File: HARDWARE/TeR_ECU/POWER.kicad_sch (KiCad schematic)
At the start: 8 parts, among them U10 LM1117MP-3.3, U2 TSR_1-2450

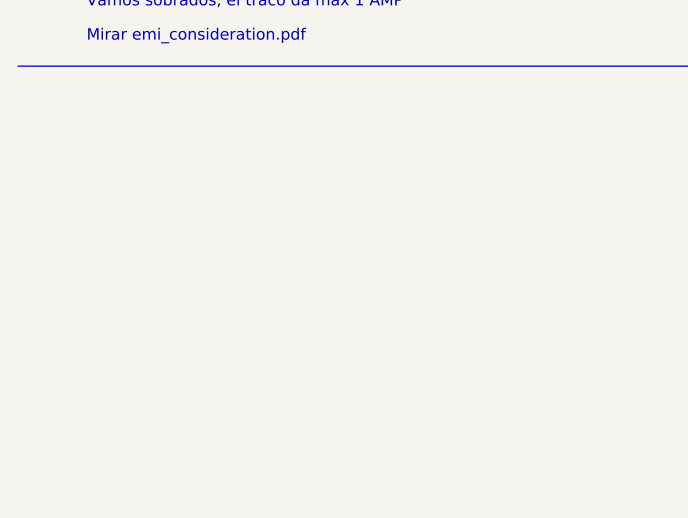
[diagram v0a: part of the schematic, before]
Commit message: Advanced design and added IMU/GPS moduleç
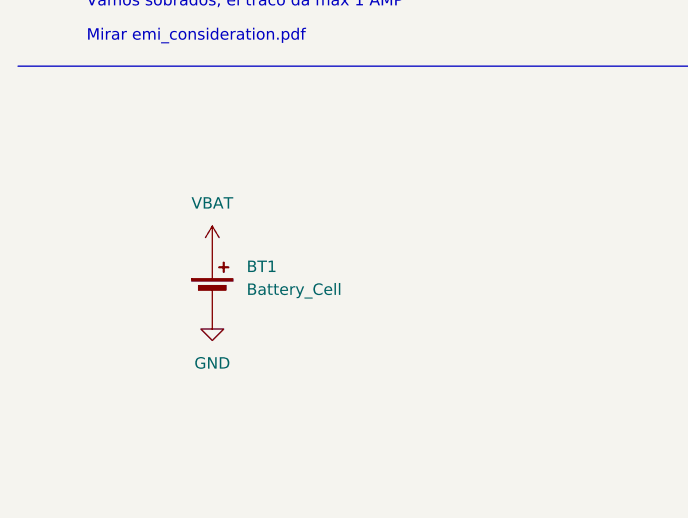
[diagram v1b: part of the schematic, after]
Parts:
- added BT1: Battery_Cell, symbol Device:Battery_Cell
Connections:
- net GND: now also BT1.2 (-)
- new net VBAT: BT1.1 (+)
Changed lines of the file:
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@@
 			(project "TeR_ECU"
 				(path "/84413845-c4f3-4743-bcd2-a67649c90902/b76a95f3-584c-4daf-bbe9-70945b593e94"
-					(reference "#PWR05")
+					(reference "#PWR033")
 					(unit 1)
 				)
@@
 			(project "TeR_ECU"
 				(path "/84413845-c4f3-4743-bcd2-a67649c90902/b76a95f3-584c-4daf-bbe9-70945b593e94"
-					(reference "U5")
+					(reference "U3")
 					(unit 1)
 				)
@@
 			(project "TeR_ECU"
 				(path "/84413845-c4f3-4743-bcd2-a67649c90902/b76a95f3-584c-4daf-bbe9-70945b593e94"
-					(reference "C22")
+					(reference "C12")
 					(unit 1)
 				)
@@
 			(project "TeR_ECU"
 				(path "/84413845-c4f3-4743-bcd2-a67649c90902/b76a95f3-584c-4daf-bbe9-70945b593e94"
-					(reference "#PWR044")
+					(reference "#PWR030")
+					(unit 1)
+				)
+			)
+		)
+	)
+	(symbol
+		(lib_name "GND_1")
+		(lib_id "power:GND")
+		(at 34.29 96.52 0)
+		(unit 1)
+		(exclude_from_sim no)
+		(in_bom yes)
+		(on_board yes)
+		(dnp no)
+		(fields_autoplaced yes)
+		(property "Reference" "#PWR036"
+			(at 34.29 102.87 0)
+			(effects
+				(font
+					(size 1.27 1.27)
+				)
+				(hide yes)
+			)
+		)
+		(property "Value" "GND"
+			(at 34.29 101.6 0)
+			(effects
+				(font
+					(size 1.27 1.27)
+				)
+			)
+		)
+		(property "Footprint" ""
+			(at 34.29 96.52 0)
+			(effects
+				(font
+					(size 1.27 1.27)
+				)
+				(hide yes)
+			)
+		)
+		(property "Datasheet" ""
+			(at 34.29 96.52 0)
+			(effects
+				(font
+					(size 1.27 1.27)
+				)
+				(hide yes)
+			)
+		)
+		(property "Description" "Power symbol creates a global label with name \"GND\" , ground"
+			(at 34.29 96.52 0)
+			(effects
+				(font
+					(size 1.27 1.27)
+				)
+				(hide yes)
+			)
+		)
+		(pin "1"
+		)
+		(instances
+			(project ""
+				(path "/84413845-c4f3-4743-bcd2-a67649c90902/b76a95f3-584c-4daf-bbe9-70945b593e94"
+					(reference "#PWR036")
 					(unit 1)
 				)
@@
 			(project "TeR_ECU"
 				(path "/84413845-c4f3-4743-bcd2-a67649c90902/b76a95f3-584c-4daf-bbe9-70945b593e94"
-					(reference "#PWR06")
+					(reference "#PWR037")
+					(unit 1)
+				)
+			)
+		)
+	)
+	(symbol
+		(lib_id "Device:Battery_Cell")
+		(at 34.29 93.98 0)
+		(unit 1)
+		(exclude_from_sim no)
+		(in_bom yes)
+		(on_board yes)
+		(dnp no)
+		(fields_autoplaced yes)
+		(property "Reference" "BT1"
+			(at 38.1 90.8684 0)
+			(effects
+				(font
+					(size 1.27 1.27)
+				)
+				(justify left)
+			)
+		)
+		(property "Value" "Battery_Cell"
+			(at 38.1 93.4084 0)
+			(effects
+				(font
+					(size 1.27 1.27)
+				)
+				(justify left)
+			)
+		)
+		(property "Footprint" ""
+			(at 34.29 92.456 90)
+			(effects
+				(font
+					(size 1.27 1.27)
+				)
+				(hide yes)
+			)
+		)
+		(property "Datasheet" "~"
+			(at 34.29 92.456 90)
+			(effects
+				(font
+					(size 1.27 1.27)
+				)
+				(hide yes)
+			)
+		)
+		(property "Description" "Single-cell battery"
+			(at 34.29 93.98 0)
+			(effects
+				(font
+					(size 1.27 1.27)
+				)
+				(hide yes)
+			)
+		)
+		(pin "1"
+		)
+		(pin "2"
+		)
+		(instances
+			(project ""
+				(path "/84413845-c4f3-4743-bcd2-a67649c90902/b76a95f3-584c-4daf-bbe9-70945b593e94"
+					(reference "BT1")
 					(unit 1)
 				)
@@
 			(project "TeR_ECU"
 				(path "/84413845-c4f3-4743-bcd2-a67649c90902/b76a95f3-584c-4daf-bbe9-70945b593e94"
-					(reference "C19")
+					(reference "C9")
 					(unit 1)
 				)
@@
 			(project "TeR_ECU"
 				(path "/84413845-c4f3-4743-bcd2-a67649c90902/b76a95f3-584c-4daf-bbe9-70945b593e94"
-					(reference "#PWR046")
+					(reference "#PWR032")
 					(unit 1)
 				)
@@
 			(project "TeR_ECU"
 				(path "/84413845-c4f3-4743-bcd2-a67649c90902/b76a95f3-584c-4daf-bbe9-70945b593e94"
-					(reference "C20")
+					(reference "C10")
 					(unit 1)
 				)
@@
 			(project "TeR_ECU"
 				(path "/84413845-c4f3-4743-bcd2-a67649c90902/b76a95f3-584c-4daf-bbe9-70945b593e94"
-					(reference "#PWR07")
+					(reference "#PWR034")
 					(unit 1)
 				)
@@
 			(project "TeR_ECU"
 				(path "/84413845-c4f3-4743-bcd2-a67649c90902/b76a95f3-584c-4daf-bbe9-70945b593e94"
-					(reference "#PWR042")
+					(reference "#PWR028")
 					(unit 1)
 				)
@@
 			(project "TeR_ECU"
 				(path "/84413845-c4f3-4743-bcd2-a67649c90902/b76a95f3-584c-4daf-bbe9-70945b593e94"
-					(reference "C21")
+					(reference "C11")
 					(unit 1)
 				)
@@
 			(project "TeR_ECU"
 				(path "/84413845-c4f3-4743-bcd2-a67649c90902/b76a95f3-584c-4daf-bbe9-70945b593e94"
-					(reference "#PWR039")
+					(reference "#PWR027")
 					(unit 1)
 				)
@@
 			(project "TeR_ECU"
 				(path "/84413845-c4f3-4743-bcd2-a67649c90902/b76a95f3-584c-4daf-bbe9-70945b593e94"
-					(reference "U1")
+					(reference "U4")
 					(unit 1)
 				)
@@
 	)
 	(symbol
+		(lib_id "power:VCC")
+		(at 34.29 88.9 0)
+		(unit 1)
+		(exclude_from_sim no)
+		(in_bom yes)
+		(on_board yes)
+		(dnp no)
+		(fields_autoplaced yes)
+		(property "Reference" "#PWR035"
+			(at 34.29 92.71 0)
+			(effects
+				(font
+					(size 1.27 1.27)
+				)
+				(hide yes)
+			)
+		)
+		(property "Value" "VBAT"
+			(at 34.29 83.82 0)
+			(effects
+				(font
+					(size 1.27 1.27)
+				)
+			)
+		)
+		(property "Footprint" ""
+			(at 34.29 88.9 0)
+			(effects
+				(font
+					(size 1.27 1.27)
+				)
+				(hide yes)
+			)
+		)
+		(property "Datasheet" ""
+			(at 34.29 88.9 0)
+			(effects
+				(font
+					(size 1.27 1.27)
+				)
+				(hide yes)
+			)
+		)
+		(property "Description" "Power symbol creates a global label with name \"VBAT\""
+			(at 34.29 88.9 0)
+			(effects
+				(font
+					(size 1.27 1.27)
+				)
+				(hide yes)
+			)
+		)
+		(pin "1"
+		)
+		(instances
+			(project ""
+				(path "/84413845-c4f3-4743-bcd2-a67649c90902/b76a95f3-584c-4daf-bbe9-70945b593e94"
+					(reference "#PWR035")
+					(unit 1)
+				)
+			)
+		)
+	)
+	(symbol
 		(lib_id "power:+24V")
 		(at 180.975 39.37 270)
@@
 			(project "TeR_ECU"
 				(path "/84413845-c4f3-4743-bcd2-a67649c90902/b76a95f3-584c-4daf-bbe9-70945b593e94"
-					(reference "#PWR049")
+					(reference "#PWR029")
 					(unit 1)
 				)
@@
 			(project "TeR_ECU"
 				(path "/84413845-c4f3-4743-bcd2-a67649c90902/b76a95f3-584c-4daf-bbe9-70945b593e94"
-					(reference "#PWR045")
-					(unit 1)
-				)
+					(reference "#PWR031")
+					(unit 1)
+				)

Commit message: Cool things
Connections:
- net 24V_IN renamed 24_VIN
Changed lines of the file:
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@@
 		(color 0 0 0 0)
 	)
+	(wire
+		(pts
+			(xy 151.13 39.37) (xy 161.29 39.37)
+		)
+		(stroke
+			(width 0)
+			(type default)
+		)
+	)
 	(polyline
 		(pts
@@
 		(pts
 			(xy 46.99 45.72) (xy 46.99 41.91)
-		)
-		(stroke
-			(width 0)
-			(type default)
-		)
-	)
-	(wire
-		(pts
-			(xy 161.29 39.37) (xy 151.765 39.37)
 		)
 		(stroke
@@
 		)
 	)
-	(hierarchical_label "24V_IN"
+	(global_label "24_VIN"
 		(shape input)
-		(at 151.765 39.37 180)
+		(at 151.13 39.37 180)
 		(fields_autoplaced yes)
 		(effects
@@
 			(justify right)
 		)
-	)
+		(property "Intersheetrefs" "${INTERSHEET_REFS}"
+			(at 141.7343 39.37 0)
+			(effects
+				(font
+					(size 1.27 1.27)
+				)
+				(justify right)
+				(hide yes)
+			)
+		)
+	)

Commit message: Quick changes, go to start layouting
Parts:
- removed BT1: Battery_Cell, symbol Device:Battery_Cell
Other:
- note removed: "Vamos sobrados, el traco da max 1 AMP"
- moved on the sheet: C10, C23, C24, C9, F1, L1, U10, U2

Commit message: First layout prototype
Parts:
- F1: footprint Fuse:Fuse_0805_2012Metric -> Fuse:Fuse_1210_3225Metric
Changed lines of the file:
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@@
 			)
 		)
-		(property "Footprint" "Fuse:Fuse_0805_2012Metric"
+		(property "Footprint" "Fuse:Fuse_1210_3225Metric"
 			(at 52.07 86.36 0)
 			(effects

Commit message: Finished layout, RF design, and quick DRC check, Lookin gud
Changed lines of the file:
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@@
-	)
-	(junction
-		(at 173.99 91.44)
-		(diameter 0)
-		(color 0 0 0 0)
 	)
 	(junction
@@
 	)
 	(junction
+		(at 140.97 91.44)
+		(diameter 0)
+		(color 0 0 0 0)
+	)
+	(junction
 		(at 109.22 91.44)
 		(diameter 0)
@@
 	(wire
 		(pts
-			(xy 163.83 91.44) (xy 173.99 91.44)
+			(xy 163.83 91.44) (xy 186.69 91.44)
 		)
 		(stroke
@@
 	(wire
 		(pts
-			(xy 173.99 91.44) (xy 186.69 91.44)
-		)
-		(stroke
-			(width 0)
-			(type default)
-		)
-	)
-	(wire
-		(pts
 			(xy 250.19 95.25) (xy 250.19 96.52)
 		)
@@
 	(wire
 		(pts
-			(xy 134.62 91.44) (xy 143.51 91.44)
+			(xy 134.62 91.44) (xy 140.97 91.44)
 		)
 		(stroke
@@
 	(wire
 		(pts
+			(xy 140.97 86.36) (xy 140.97 91.44)
+		)
+		(stroke
+			(width 0)
+			(type default)
+		)
+	)
+	(wire
+		(pts
 			(xy 214.63 85.09) (xy 214.63 86.36)
 		)
@@
 		(pts
 			(xy 116.84 102.87) (xy 116.84 99.06)
+		)
+		(stroke
+			(width 0)
+			(type default)
+		)
+	)
+	(wire
+		(pts
+			(xy 140.97 91.44) (xy 143.51 91.44)
 		)
 		(stroke
@@
 	)
 	(symbol
+		(lib_id "power:PWR_FLAG")
+		(at 140.97 86.36 0)
+		(unit 1)
+		(exclude_from_sim no)
+		(in_bom yes)
+		(on_board yes)
+		(dnp no)
+		(property "Reference" "#FLG02"
+			(at 140.97 84.455 0)
+			(effects
+				(font
+					(size 1.27 1.27)
+				)
+				(hide yes)
+			)
+		)
+		(property "Value" "PWR_FLAG"
+			(at 140.97 82.55 0)
+			(effects
+				(font
+					(size 1.27 1.27)
+				)
+			)
+		)
+		(property "Footprint" ""
+			(at 140.97 86.36 0)
+			(effects
+				(font
+					(size 1.27 1.27)
+				)
+				(hide yes)
+			)
+		)
+		(property "Datasheet" "~"
+			(at 140.97 86.36 0)
+			(effects
+				(font
+					(size 1.27 1.27)
+				)
+				(hide yes)
+			)
+		)
+		(property "Description" ""
+			(at 140.97 86.36 0)
+			(effects
+				(font
+					(size 1.27 1.27)
+				)
+				(hide yes)
+			)
+		)
+		(pin "1"
+		)
+		(instances
+			(project "TeR_ECU"
+				(path "/84413845-c4f3-4743-bcd2-a67649c90902/b76a95f3-584c-4daf-bbe9-70945b593e94"
+					(reference "#FLG02")
+					(unit 1)
+				)
+			)
+		)
+	)
+	(symbol
 		(lib_id "Device:C")
 		(at 223.52 91.44 0)
@@
 					(unit 1)
 				)
-			)
-		)
-	)
-	(symbol
-		(lib_id "power:PWR_FLAG")
-		(at 173.99 91.44 0)
-		(unit 1)
-		(exclude_from_sim no)
-		(in_bom yes)
-		(on_board yes)
-		(dnp no)
-		(property "Reference" "#FLG03"
-			(at 173.99 89.535 0)
-			(effects
-				(font
-					(size 1.27 1.27)
-				)
-				(hide yes)
-			)
-		)
-		(property "Value" "PWR_FLAG"
-			(at 173.99 87.63 0)
-			(effects
-				(font
-					(size 1.27 1.27)
-				)
-			)
-		)
-		(property "Footprint" ""
-			(at 173.99 91.44 0)
-			(effects
-				(font
-					(size 1.27 1.27)
-				)
-				(hide yes)
-			)
-		)
-		(property "Datasheet" "~"
-			(at 173.99 91.44 0)
-			(effects
-				(font
-					(size 1.27 1.27)
-				)
-				(hide yes)
-			)
-		)
-		(property "Description" ""
-			(at 173.99 91.44 0)
-			(effects
-				(font
-					(size 1.27 1.27)
-				)
-				(hide yes)
-			)
-		)
-		(pin "1"
-		)
-		(instances
-			(project "TER_PEDAL"
-				(path "/73ede3a3-6344-40fe-9207-10ff50d388ba/6f10bd65-583f-4818-aeb8-8b5e6e37f336"
-					(reference "#FLG03")
-					(unit 1)
-				)
-			)
-			(project "TeR_ECU"
-				(path "/84413845-c4f3-4743-bcd2-a67649c90902/b76a95f3-584c-4daf-bbe9-70945b593e94"
-					(reference "#FLG02")
-					(unit 1)
-				)
